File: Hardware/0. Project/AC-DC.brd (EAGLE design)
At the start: 100 x 75 mm, 91 parts, among them IC1 7824TV, IC2 7812TV, IC3 LM324D, IC4 LM358D, K1 12VDC COIL, K2 12VDC COIL, K3 12VDC COIL, K4 12VDC COIL, Q1 BC848SMD, Q2 BC848BSMD, Q3 BC858BSMD, Q4 BC858BSMD, Q5 BC858BSMD, Q6 BC858BSMD, U1 LM338K, U2 LM338K

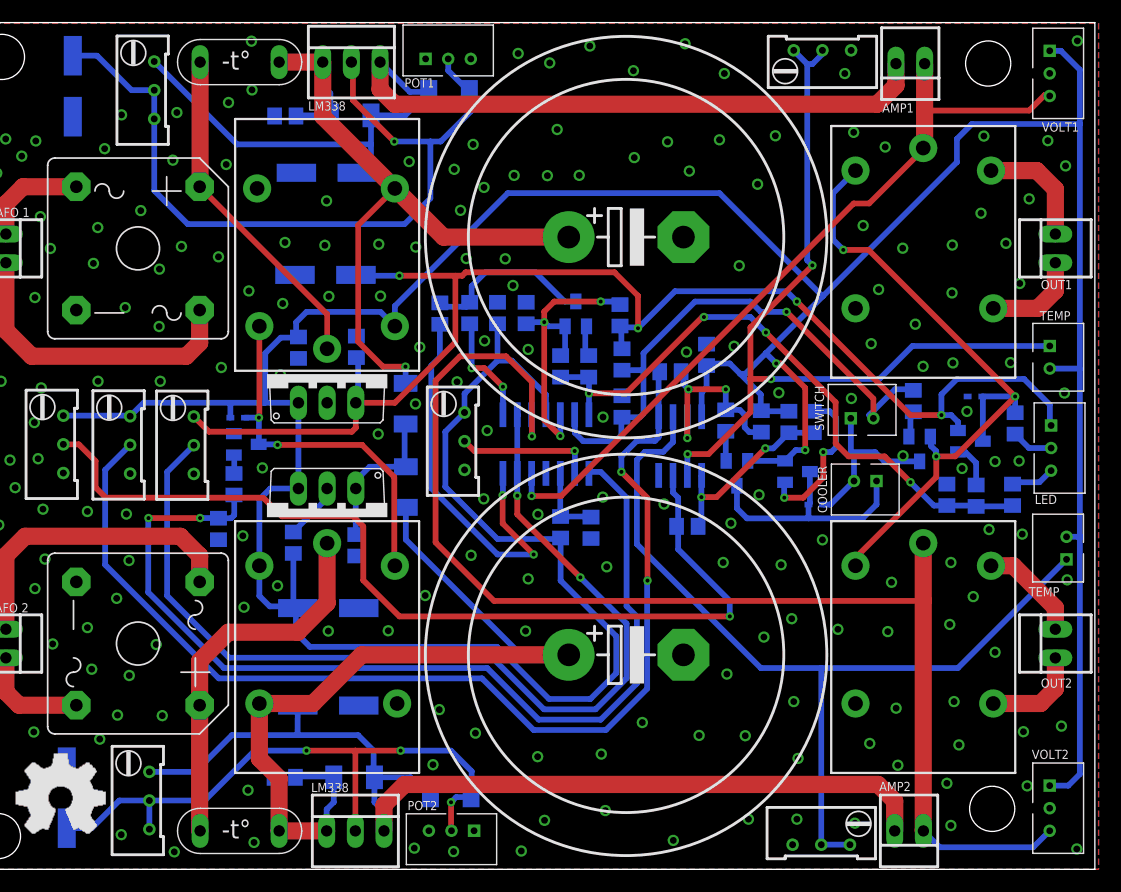
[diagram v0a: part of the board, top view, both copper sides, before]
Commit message: GND high current return improved
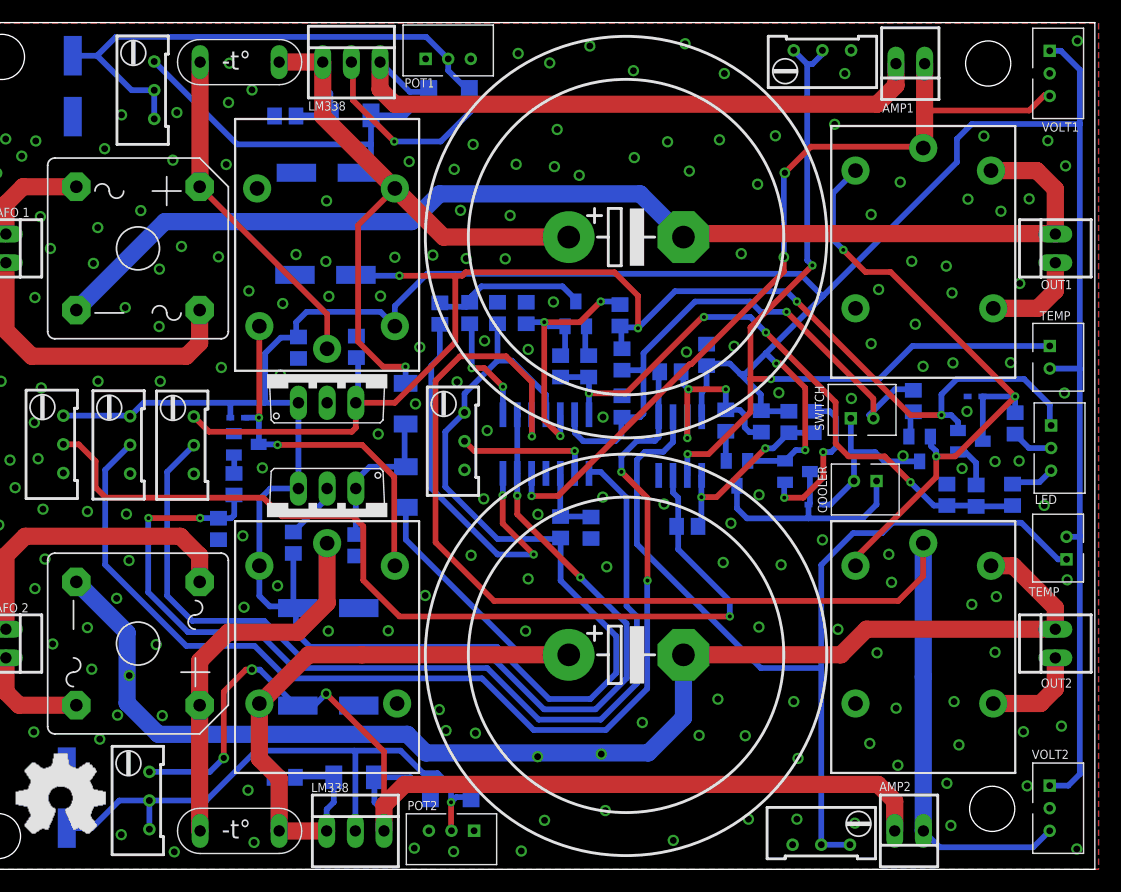
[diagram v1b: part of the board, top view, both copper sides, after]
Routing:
- net 0V: track 40.3 -> 237.4 mm, vias 201 -> 199
- net N$15: track 89.3 -> 101.3 mm, vias 0 -> 3
- net N$31: track 78.3 -> 86.4 mm
- net +24V: track 345.7 -> 339.6 mm
- net N$27: track 71.0 -> 65.6 mm
- net SHORT_CIRCUIT_MONITOR_2: track 68.7 -> 73.9 mm, vias 1 -> 3
- net SHORT_CIRCUIT_MONITOR_1: track 114.6 -> 118.5 mm
- net N$16: track 55.8 -> 53.8 mm, vias 3 -> 1
- net !SHORT_CIRCUIT_DETECTED!: track 15.5 -> 14.0 mm
- net N$21: track 27.1 -> 26.5 mm

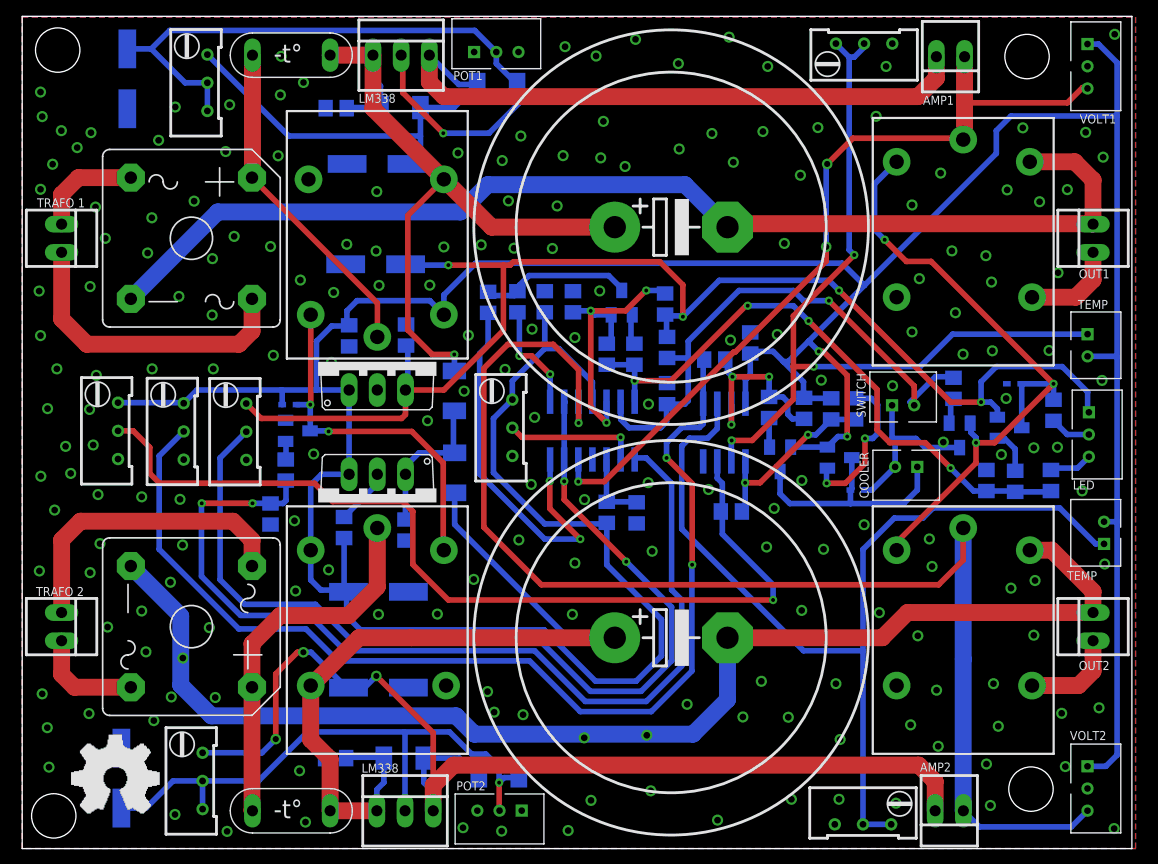
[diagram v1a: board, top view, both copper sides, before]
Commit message: Components designators repositioned
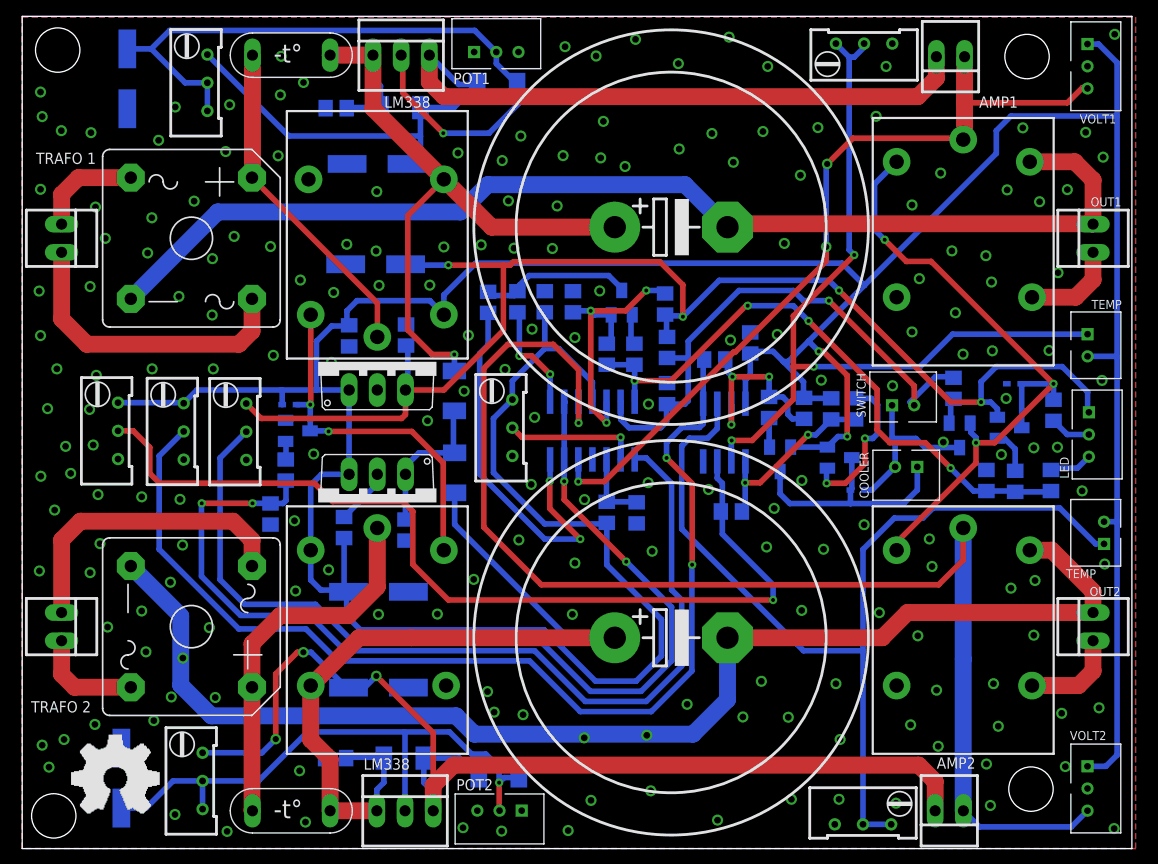
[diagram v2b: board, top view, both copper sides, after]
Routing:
- net 0V: vias 199 -> 197
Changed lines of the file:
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@@
 <layer number="17" name="Pads" color="2" fill="1" visible="yes" active="yes"/>
 <layer number="18" name="Vias" color="2" fill="1" visible="yes" active="yes"/>
-<layer number="19" name="Unrouted" color="6" fill="1" visible="no" active="yes"/>
-<layer number="20" name="Dimension" color="24" fill="1" visible="no" active="yes"/>
-<layer number="21" name="tPlace" color="7" fill="1" visible="no" active="yes"/>
-<layer number="22" name="bPlace" color="7" fill="1" visible="no" active="yes"/>
-<layer number="23" name="tOrigins" color="15" fill="1" visible="no" active="yes"/>
-<layer number="24" name="bOrigins" color="15" fill="1" visible="no" active="yes"/>
-<layer number="25" name="tNames" color="7" fill="1" visible="no" active="yes"/>
-<layer number="26" name="bNames" color="7" fill="1" visible="no" active="yes"/>
-<layer number="27" name="tValues" color="7" fill="1" visible="no" active="yes"/>
-<layer number="28" name="bValues" color="7" fill="1" visible="no" active="yes"/>
-<layer number="29" name="tStop" color="7" fill="3" visible="no" active="yes"/>
-<layer number="30" name="bStop" color="7" fill="6" visible="no" active="yes"/>
+<layer number="19" name="Unrouted" color="6" fill="1" visible="yes" active="yes"/>
+<layer number="20" name="Dimension" color="24" fill="1" visible="yes" active="yes"/>
+<layer number="21" name="tPlace" color="7" fill="1" visible="yes" active="yes"/>
+<layer number="22" name="bPlace" color="7" fill="1" visible="yes" active="yes"/>
+<layer number="23" name="tOrigins" color="15" fill="1" visible="yes" active="yes"/>
+<layer number="24" name="bOrigins" color="15" fill="1" visible="yes" active="yes"/>
+<layer number="25" name="tNames" color="7" fill="1" visible="yes" active="yes"/>
+<layer number="26" name="bNames" color="7" fill="1" visible="yes" active="yes"/>
+<layer number="27" name="tValues" color="7" fill="1" visible="yes" active="yes"/>
+<layer number="28" name="bValues" color="7" fill="1" visible="yes" active="yes"/>
+<layer number="29" name="tStop" color="7" fill="3" visible="yes" active="yes"/>
+<layer number="30" name="bStop" color="7" fill="6" visible="yes" active="yes"/>
 <layer number="31" name="tCream" color="7" fill="4" visible="no" active="yes"/>
 <layer number="32" name="bCream" color="7" fill="5" visible="no" active="yes"/>
@@
 <rectangle x1="7.77875" y1="10.09015" x2="9.02335" y2="10.17905" layer="21"/>
 <rectangle x1="7.77875" y1="10.17905" x2="9.02335" y2="10.26795" layer="21"/>
-<text x="1.3335" y="57.785" size="0.8128" layer="21" font="vector" ratio="17">TRAFO 1</text>
-<text x="1.2446" y="22.7584" size="0.8128" layer="21" font="vector" ratio="17">TRAFO 2</text>
-<text x="30.5816" y="6.8453" size="0.8128" layer="21" font="vector" ratio="17">LM338</text>
-<text x="30.3149" y="67.2084" size="0.8128" layer="21" font="vector" ratio="17">LM338</text>
-<text x="38.8493" y="69.2531" size="0.8128" layer="21" font="vector" ratio="17">POT1</text>
-<text x="39.116" y="5.2451" size="0.8128" layer="21" font="vector" ratio="17">POT2</text>
-<text x="81.1657" y="67.0306" size="0.8128" layer="21" font="vector" ratio="17">AMP1</text>
-<text x="80.899" y="6.9342" size="0.8128" layer="21" font="vector" ratio="17">AMP2</text>
-<text x="95.2119" y="51.3842" size="0.8128" layer="21" font="vector" ratio="17">OUT1</text>
-<text x="95.2119" y="16.0909" size="0.8128" layer="21" font="vector" ratio="17">OUT2</text>
+<text x="1.2446" y="61.6966" size="1.016" layer="21" font="vector" ratio="17">TRAFO 1</text>
+<text x="0.8001" y="12.2682" size="1.016" layer="21" font="vector" ratio="18">TRAFO 2</text>
+<text x="30.7594" y="7.112" size="1.016" layer="21" font="vector" ratio="17">LM338</text>
+<text x="32.6263" y="66.7639" size="1.016" layer="21" font="vector" ratio="17">LM338</text>
+<text x="38.8493" y="68.8975" size="1.016" layer="21" font="vector" ratio="17">POT1</text>
+<text x="39.116" y="5.2451" size="1.016" layer="21" font="vector" ratio="17">POT2</text>
+<text x="86.233" y="66.7639" size="1.016" layer="21" font="vector" ratio="17">AMP1</text>
+<text x="82.4103" y="7.2009" size="1.016" layer="21" font="vector" ratio="17">AMP2</text>
+<text x="96.2787" y="57.8739" size="0.8128" layer="21" font="vector" ratio="17">OUT1</text>
+<text x="96.1898" y="22.7584" size="0.8128" layer="21" font="vector" ratio="17">OUT2</text>
 <text x="95.3008" y="65.3415" size="0.8128" layer="21" font="vector" ratio="17">VOLT1</text>
 <text x="94.4118" y="9.779" size="0.8128" layer="21" font="vector" ratio="17">VOLT2</text>
-<text x="94.6785" y="32.3596" size="0.8128" layer="21" font="vector" ratio="17">LED</text>
-<text x="95.123" y="48.6283" size="0.8128" layer="21" font="vector" ratio="17">TEMP</text>
+<text x="94.3229" y="33.3375" size="0.8128" layer="21" font="vector" ratio="17" rot="R90">LED</text>
+<text x="96.3676" y="48.6283" size="0.8128" layer="21" font="vector" ratio="17">TEMP</text>
 <text x="76.2762" y="31.5595" size="0.8128" layer="21" font="vector" ratio="17" rot="R90">COOLER</text>
-<text x="94.1451" y="24.1808" size="0.8128" layer="21" font="vector" ratio="17">TEMP</text>
+<text x="94.0562" y="24.3586" size="0.8128" layer="21" font="vector" ratio="17">TEMP</text>
 <text x="76.0095" y="38.8493" size="0.8128" layer="21" font="vector" ratio="17" rot="R90">SWITCH</text>
 <polygon width="0.0254" layer="29">
@@
 <via x="17.2212" y="43.2308" extent="1-16" drill="0.6"/>
 <via x="1.651" y="59.4106" extent="1-16" drill="0.6"/>
-<via x="2.7432" y="61.6712" extent="1-16" drill="0.6"/>
-<via x="4.953" y="63.1698" extent="1-16" drill="0.6"/>
 <via x="12.2936" y="63.8302" extent="1-16" drill="0.6"/>
 <via x="15.494" y="58.3438" extent="1-16" drill="0.6"/>
@@
 <via x="11.8618" y="11.5316" extent="1-16" drill="0.6"/>
 <via x="2.413" y="7.3406" extent="1-16" drill="0.6"/>
-<via x="2.2606" y="10.8966" extent="1-16" drill="0.6"/>
-<via x="6.0198" y="12.1666" extent="1-16" drill="0.6"/>
+<via x="3.7719" y="9.8298" extent="1-16" drill="0.6"/>
+<via x="6.5532" y="11.1887" extent="1-16" drill="0.6"/>
 <via x="18.4658" y="1.5494" extent="1-16" drill="0.6"/>
-<via x="1.8034" y="13.9446" extent="1-16" drill="0.6"/>
+<via x="1.8034" y="9.3218" extent="1-16" drill="0.6"/>
 <via x="1.5494" y="25.019" extent="1-16" drill="0.6"/>
 <via x="1.8034" y="65.9638" extent="1-16" drill="0.6"/>

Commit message: Schematic updated to 2.0
- All Op. Amps. that was voltage compators was updated to LM393.
- Fixed conflicts at +12V and +24V lines.
- Now, there is only one temperature circuit monitor.
- Ground from supply1 and supply2 is now isolated from each other
(series and parallel association are now possible).
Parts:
- removed C1, C16, C2, C3: 100nF x 50V, rcl:C0805
- removed C10: (no value), rcl:C0805
- removed C4: 10uF x 50V, rcl:153CLV-0605
- removed IC1: 7824TV, linear:TO220V
- removed IC2: 7812TV, linear:TO220V
- removed IC3: LM324D, linear:SO14
- removed Q5: BC858BSMD, transistor-pnp:SOT23-BEC
- removed R15, R17: 10k, rcl:RTRIM64W
- removed R22: 33k (5%), rcl:R0805
- removed R30, R32: 10k (5%), rcl:R0805
- removed RT3: 10k, ptc-ntc:MOLEX2P
- added D10: (no value), diode:SOD80C
- added IC5, IC6: LM393D, linear:SO08
- added OK1, OK2, OK3, OK4: 4N33, optocoupler:DIL06
- added Q7: BC848SMD, transistor-npn:SOT23
- added R35, R38, R46, R49: 100k (5%), rcl:R0805
- added R36, R44, R48: 1k (5%), rcl:R0805
- added R37, R39, R43, R47: 10k (5%), rcl:R0805
- added R40: 500k, rcl:RTRIM64W
- added R41: 100k (1%), rcl:R0805
- added R42: 33k (1%), rcl:R0805
- added R45, R50: (no value), rcl:R2512
- added U3: HLK-PM01, HLK-PM01:HLK-PM01
- D8: value 1N4007 -> 1N4148; device diode:SOD-123_MINI-SMA -> diode:SOD523
- D9: value 1N4007 -> (none); device diode:SOD-123_MINI-SMA -> diode:SOD80C
- R10: value 1k (5%) -> 10k (5%)
- R5: value 10k (5%) -> 500k; device rcl:R0805 -> rcl:RTRIM64W
- TR1, TR2: value TRAFO -> 24VRMS
- moved D8 234.3 mm to (-42.0, -186.1), flipped to the top, turned to 0 degrees
- moved K1 208.2 mm to (-31.6, -143.2), turned to 0 degrees
- moved R5 193.5 mm to (-28.9, -156.5), flipped to the top, turned to 0 degrees
- moved D9 187.1 mm to (-40.6, -128.1), flipped to the top, turned to 0 degrees
- moved R11 118.9 mm to (-30.2, -45.3), flipped to the top, turned to 0 degrees
- moved R10 115.8 mm to (-30.2, -39.0), flipped to the top, turned to 0 degrees
- moved C6 45.8 mm to (59.2, 89.4)
- moved D2 13.4 mm to (34.4, -5.27)
- moved C8 11.9 mm to (27.3, -3.67)
- moved D4 11.5 mm to (34.3, 78.2)
- moved C13 11.1 mm to (28.0, 77.8)
- moved D5 10.9 mm to (42.6, 79.8)
- moved D3 9.97 mm to (43.4, -3.40)
- moved AMP1 3.41 mm to (86.9, 3.85)
- moved R26 2.87 mm to (12.6, 69.4)
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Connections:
- removed net 0V: B1.-, B2.-, C1.2, C10.2, C11.-, C12.-, C13.2, C14.-, C15.-, C16.2, C2.2, C3.2, C4.-, C5.2, C6.-, C7.-, C8.2, C9.-, D6.A, D7.A, IC1.2, IC2.2, IC3.11, IC4.4, K3.A2, K4.A2, L1.P$2, Q1.2, Q3.C, R1.1, R14.P$1, R14.P$3, R15.1, R17.1, R19.1, R21.1, R27.P$1, R27.P$3, R33.2, R4.1, R5.1, R7.1, R8.1, R9.1, S2.P$1, VOLT1.P$2, VOLT2.P$2, X1.2, X2.2
- removed net 12V: C5.1, C6.+, IC2.3, LED1.P$1, Q6.E, R18.2, R20.2, R7.3
- removed net 30V: C1.1, D8.C, D9.C, IC1.1
- removed net 30V_A: C7.+, C8.1, D2.C, D8.A, K2.14, RT1.P$1, U1.1
- removed net 30V_B: C12.+, C13.1, D4.C, D9.A, K1.14, RT4.P$1, U2.1
- removed net HIGH_TEMPERATURE_2: IC4.7, R22.2, R30.1, R32.1
- removed net N$30: IC4.5, R15.2, R22.1
- removed net N$31: IC4.6, R17.2, R17.3, RT3.P$1
- removed net N$34: Q5.B, R32.2
- removed net SHORT_CIRCUIT_MONITOR_1: AMP1.1, IC3.3, K4.11, VOLT1.P$3
- removed net SHORT_CIRCUIT_MONITOR_2: AMP2.1, IC3.12, K3.11, VOLT2.P$3
- new net !VOUT1_POWER_ON!1: OK1.5, R11.1
- new net !VOUT1_POWER_ON!2: OK2.5, R36.1
- new net !VOUT1_POWER_ON!3: OK3.5, R44.1
- new net !VOUT1_POWER_ON!4: OK4.5, R48.1
- new net +12V: C5.1, C6.+, D1.C, D8.C, IC4.8, K1.A1, K2.A1, LED1.P$1, Q4.E, Q6.E, R11.2, R18.2, R20.2, R28.2, R36.2, R44.2, R48.2, R8.3, RT2.P$2, U3.P$4
- new net 0V_B: U3.P$2
- new net 127V_B: U3.P$1
- new net 12V_AUX1: D9.C, IC5.8, R1.3, R45.1, R7.3
- new net 12V_AUX2: D10.C, IC6.8, R40.3, R5.3, R50.1
- new net C_FULL_1: C7.+, C8.1, D2.C, K2.14, R3.2, R45.2, RT1.P$1, U1.1
- new net C_FULL_2: C12.+, C13.1, D4.C, K1.14, R41.2, R50.2, RT4.P$1, U2.1
- new net GND1: B1.-, C11.-, C7.-, C8.2, C9.-, D9.A, IC5.4, OK1.2, OK2.2, R1.1, R14.P$1, R14.P$3, R33.2, R4.1, R7.1, VOLT1.P$2, X1.2
- new net GND2: B2.-, C12.-, C13.2, C14.-, C15.-, D10.A, IC6.4, OK3.2, OK4.2, R27.P$1, R27.P$3, R40.1, R42.1, R5.1, VOLT2.P$2, X2.2
- new net HIGH_TEMPERATURE: IC4.1, R12.2
- new net N$33: D8.A, K1.A2, Q7.3
- new net N$37: IC5.7, R37.1
- new net N$39: OK2.1, R37.2
- new net N$40: Q7.1, R39.2
- new net N$41: IC6.5, R41.1, R42.2
- new net N$42: IC6.1, R43.1
- new net N$43: IC6.6, R40.2
- new net N$44: OK3.1, R43.2
- new net N$45: IC6.7, R47.1
- new net N$46: OK4.1, R47.2
- new net N$47: OK4.4, R39.1, R49.2
- new net N$48: OK2.4, R38.2, R6.1
- new net PE: C5.2, C6.-, D6.A, D7.A, IC4.4, K3.A2, K4.A2, L1.P$2, Q1.2, Q3.C, Q7.2, R19.1, R21.1, R35.1, R38.1, R46.1, R49.1, R8.1, R9.1, S2.P$1, U3.P$3
- new net VOUT_1: AMP1.1, IC5.3, IC6.3, K4.11, VOLT1.P$3
- new net VOUT_2: AMP2.1, K3.11, VOLT2.P$3
- net !SHORT_CIRCUIT_DETECTED!: now also OK1.4, OK3.4, R35.2, R46.2; no longer R10.2, R11.2
- net !VOUT1_POWER_OFF!: now also IC4.7; no longer IC3.7
- net !VOUT1_POWER_ON!: now also IC4.6; no longer IC3.6
- net +24V: no longer C10.1, C16.1, C2.1, C3.1, C4.+, D1.C, IC1.3, IC2.1, IC3.4, IC4.8, K1.A1, K2.A1, Q4.E, Q5.E, R1.3, R15.3, R28.2, R3.2, R30.2, R8.3, RT2.P$2, RT3.P$2
- net HIGH_TEMPERATURE_1: no longer IC4.1, R12.2
- net N$18: now also IC5.5; no longer IC3.10
- net N$19: now also IC5.1; no longer IC3.1
- net N$2: no longer K1.A2
- net N$20: now also OK1.1, R10.2; no longer IC3.14, R11.1
- net N$21: now also IC4.5; no longer IC3.5
- net N$25: now also IC5.2; no longer IC3.13, IC3.2
- net N$38: no longer Q5.C
- net N$5: now also IC6.2; no longer IC3.8, R6.1
- net N$6: now also IC5.6; no longer IC3.9
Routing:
- net +24V: track 339.6 -> 0.00 mm
- net 0V: track 237.4 -> 0.00 mm, vias 197 -> 0
- net 12V: track 121.0 -> 0.00 mm, vias 4 -> 0
- net SHORT_CIRCUIT_MONITOR_1: track 118.5 -> 0.00 mm, vias 1 -> 0
- net GND2: track 0.00 -> 112.9 mm
- net N$30: track 98.5 -> 0.00 mm, vias 2 -> 0
- net N$25: track 87.7 -> 0.00 mm
- net N$5: track 86.6 -> 0.00 mm, vias 2 -> 0
- net N$31: track 86.4 -> 0.00 mm
- net N$36: track 84.2 -> 0.00 mm
- net 30V_A: track 75.4 -> 0.00 mm
- net C_FULL_1: track 0.00 -> 74.1 mm
- net SHORT_CIRCUIT_MONITOR_2: track 73.9 -> 0.00 mm, vias 3 -> 0
- net N$35: track 73.8 -> 0.00 mm
- net N$27: track 65.6 -> 0.65 mm, vias 1 -> 0
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- added copper zone on layer 1, net GND1
- added copper zone on layer 16, net GND1
- removed copper zone on layer 1, net 0V
- removed copper zone on layer 16, net 0V
